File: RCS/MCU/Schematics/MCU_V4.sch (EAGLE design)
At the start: 28 parts, among them IC1 FT232RL, J1 MOTOR, J2 POWER, J3 SENSORS, Q2 8 MHz, U1 ATMEGA328P_TQFP

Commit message: Updated INTEV Schematic
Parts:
- added J5: USB-MICROB, SparkFun-Connectors:USB-MICROB
- added SW1: (no value), adafruit:SWITCH_PUSHBUTTONSOFTTOUCHSMD_SJ
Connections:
- net DM: now also J5.D-
- net DP: now also J5.D+
- net GND: now also J5.GND, SW1.P$2
- net RESET: now also SW1.P$1
- net USBVDD: now also J5.VBUS
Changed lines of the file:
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@@
 <part name="J3" library="SparkFun-Connectors" deviceset="M03" device="LOCK" value="SENSORS"/>
 <part name="J4" library="SparkFun-Connectors" deviceset="M06" device="LOCK"/>
+<part name="SW1" library="adafruit" deviceset="SWITCH_PUSHBUTTON" device="SOFTTOUCHSMD_SJ"/>
+<part name="GND13" library="supply1" deviceset="GND" device=""/>
+<part name="J5" library="SparkFun-Connectors" deviceset="USB" device="-MICROB"/>
+<part name="GND14" library="supply1" deviceset="GND" device=""/>
 </parts>
 <sheets>
@@
 <instance part="J3" gate="J$1" x="-12.7" y="78.74"/>
 <instance part="J4" gate="G$1" x="-40.64" y="86.36"/>
+<instance part="SW1" gate="G$1" x="43.18" y="88.9"/>
+<instance part="GND13" gate="1" x="91.44" y="81.28"/>
+<instance part="J5" gate="G$1" x="-45.72" y="45.72" rot="R180"/>
+<instance part="GND14" gate="1" x="-30.48" y="40.64"/>
 </instances>
 <busses>
@@
 <label x="-33.02" y="81.28" size="1.27" layer="95" xref="yes"/>
 </segment>
+<segment>
+<pinref part="GND13" gate="1" pin="GND"/>
+<wire x1="48.26" y1="88.9" x2="91.44" y2="88.9" width="0.1524" layer="91"/>
+<wire x1="91.44" y1="88.9" x2="91.44" y2="83.82" width="0.1524" layer="91"/>
+<pinref part="SW1" gate="G$1" pin="P$2"/>
+</segment>
+<segment>
+<pinref part="J5" gate="G$1" pin="GND"/>
+<wire x1="-43.18" y1="45.72" x2="-30.48" y2="45.72" width="0.1524" layer="91"/>
+<wire x1="-30.48" y1="45.72" x2="-30.48" y2="43.18" width="0.1524" layer="91"/>
+<pinref part="GND14" gate="1" pin="GND"/>
+</segment>
 </net>
 <net name="VDD" class="0">
@@
 <label x="111.76" y="7.62" size="1.27" layer="95" rot="R180" xref="yes"/>
 </segment>
+<segment>
+<pinref part="J5" gate="G$1" pin="D-"/>
+<wire x1="-43.18" y1="40.64" x2="-40.64" y2="40.64" width="0.1524" layer="91"/>
+<label x="-40.64" y="40.64" size="1.27" layer="95" xref="yes"/>
+</segment>
 </net>
 <net name="DP" class="0">
@@
 <wire x1="114.3" y1="10.16" x2="111.76" y2="10.16" width="0.1524" layer="91"/>
 <label x="111.76" y="10.16" size="1.27" layer="95" rot="R180" xref="yes"/>
+</segment>
+<segment>
+<pinref part="J5" gate="G$1" pin="D+"/>
+<wire x1="-43.18" y1="38.1" x2="-40.64" y2="38.1" width="0.1524" layer="91"/>
+<label x="-40.64" y="38.1" size="1.27" layer="95" xref="yes"/>
 </segment>
 </net>
@@
 <label x="-2.54" y="76.2" size="1.27" layer="95" xref="yes"/>
 <pinref part="J3" gate="J$1" pin="1"/>
-</segment>
-</net>
-<net name="N$5" class="0">
-<segment>
-<pinref part="FLIGHT-STATE-TABLE" gate="G$1" pin="A2"/>
-<wire x1="147.32" y1="104.14" x2="139.7" y2="104.14" width="0.1524" layer="91"/>
-<wire x1="147.32" y1="104.14" x2="147.32" y2="111.76" width="0.1524" layer="91"/>
-<pinref part="FLIGHT-STATE-TABLE" gate="G$1" pin="WP"/>
-<wire x1="139.7" y1="93.98" x2="152.4" y2="93.98" width="0.1524" layer="91"/>
-<wire x1="152.4" y1="93.98" x2="152.4" y2="111.76" width="0.1524" layer="91"/>
-<wire x1="152.4" y1="111.76" x2="147.32" y2="111.76" width="0.1524" layer="91"/>
-<pinref part="R1" gate="G$1" pin="2"/>
-<wire x1="147.32" y1="111.76" x2="116.84" y2="111.76" width="0.1524" layer="91"/>
-<wire x1="20.32" y1="86.36" x2="20.32" y2="88.9" width="0.1524" layer="91"/>
-<wire x1="20.32" y1="88.9" x2="20.32" y2="91.44" width="0.1524" layer="91"/>
-<wire x1="20.32" y1="88.9" x2="101.6" y2="88.9" width="0.1524" layer="91"/>
-<wire x1="101.6" y1="88.9" x2="101.6" y2="104.14" width="0.1524" layer="91"/>
-<junction x="20.32" y="88.9"/>
-<pinref part="FLIGHT-STATE-TABLE" gate="G$1" pin="VCC"/>
-<wire x1="101.6" y1="104.14" x2="116.84" y2="104.14" width="0.1524" layer="91"/>
-<pinref part="FLIGHT-DATA-STORAGE" gate="G$1" pin="VCC"/>
-<wire x1="116.84" y1="104.14" x2="119.38" y2="104.14" width="0.1524" layer="91"/>
-<wire x1="119.38" y1="76.2" x2="101.6" y2="76.2" width="0.1524" layer="91"/>
-<wire x1="101.6" y1="76.2" x2="101.6" y2="88.9" width="0.1524" layer="91"/>
-<junction x="101.6" y="88.9"/>
-<wire x1="116.84" y1="111.76" x2="116.84" y2="104.14" width="0.1524" layer="91"/>
-<junction x="116.84" y="104.14"/>
-<junction x="147.32" y="111.76"/>
-<pinref part="R4" gate="G$1" pin="2"/>
-<wire x1="10.16" y1="93.98" x2="15.24" y2="93.98" width="0.1524" layer="91"/>
-<wire x1="15.24" y1="93.98" x2="15.24" y2="88.9" width="0.1524" layer="91"/>
-<wire x1="15.24" y1="88.9" x2="20.32" y2="88.9" width="0.1524" layer="91"/>
-<wire x1="15.24" y1="88.9" x2="15.24" y2="68.58" width="0.1524" layer="91"/>
-<junction x="15.24" y="88.9"/>
-<pinref part="U1" gate="U$1" pin="VCC@6"/>
-<pinref part="U1" gate="U$1" pin="VCC@4"/>
-<pinref part="U1" gate="U$1" pin="AVCC"/>
-<wire x1="35.56" y1="68.58" x2="33.02" y2="68.58" width="0.1524" layer="91"/>
-<wire x1="33.02" y1="68.58" x2="33.02" y2="66.04" width="0.1524" layer="91"/>
-<wire x1="33.02" y1="66.04" x2="35.56" y2="66.04" width="0.1524" layer="91"/>
-<junction x="33.02" y="66.04"/>
-<wire x1="33.02" y1="66.04" x2="33.02" y2="63.5" width="0.1524" layer="91"/>
-<wire x1="33.02" y1="63.5" x2="35.56" y2="63.5" width="0.1524" layer="91"/>
-<wire x1="15.24" y1="68.58" x2="33.02" y2="68.58" width="0.1524" layer="91"/>
-<junction x="33.02" y="68.58"/>
-<pinref part="F1" gate="1" pin="1"/>
 </segment>
 </net>
@@
 <label x="106.68" y="43.18" size="1.27" layer="95" rot="R180" xref="yes"/>
 </segment>
+<segment>
+<pinref part="J5" gate="G$1" pin="VBUS"/>
+<wire x1="-43.18" y1="43.18" x2="-40.64" y2="43.18" width="0.1524" layer="91"/>
+<label x="-40.64" y="43.18" size="1.27" layer="95" xref="yes"/>
+</segment>
 </net>
 <net name="N$9" class="0">
@@
 <wire x1="33.02" y1="81.28" x2="50.8" y2="81.28" width="0.1524" layer="91"/>
 <junction x="33.02" y="73.66"/>
+<wire x1="33.02" y1="81.28" x2="33.02" y2="88.9" width="0.1524" layer="91"/>
+<junction x="33.02" y="81.28"/>
+<pinref part="SW1" gate="G$1" pin="P$1"/>
+<wire x1="33.02" y1="88.9" x2="38.1" y2="88.9" width="0.1524" layer="91"/>
 </segment>
 </net>
@@
 </segment>
 </net>
+<net name="N$1" class="0">
+<segment>
+<pinref part="U1" gate="U$1" pin="VCC@6"/>
+<wire x1="33.02" y1="63.5" x2="35.56" y2="63.5" width="0.1524" layer="91"/>
+<pinref part="U1" gate="U$1" pin="VCC@4"/>
+<wire x1="33.02" y1="66.04" x2="35.56" y2="66.04" width="0.1524" layer="91"/>
+<junction x="33.02" y="66.04"/>
+<wire x1="33.02" y1="66.04" x2="33.02" y2="63.5" width="0.1524" layer="91"/>
+<pinref part="U1" gate="U$1" pin="AVCC"/>
+<wire x1="35.56" y1="68.58" x2="33.02" y2="68.58" width="0.1524" layer="91"/>
+<wire x1="33.02" y1="68.58" x2="33.02" y2="66.04" width="0.1524" layer="91"/>
+<junction x="33.02" y="68.58"/>
+<pinref part="F1" gate="1" pin="1"/>
+<pinref part="R1" gate="G$1" pin="2"/>
+<wire x1="20.32" y1="86.36" x2="20.32" y2="88.9" width="0.1524" layer="91"/>
+<wire x1="20.32" y1="88.9" x2="20.32" y2="91.44" width="0.1524" layer="91"/>
+<junction x="20.32" y="88.9"/>
+<pinref part="R4" gate="G$1" pin="2"/>
+<wire x1="10.16" y1="93.98" x2="15.24" y2="93.98" width="0.1524" layer="91"/>
+<wire x1="15.24" y1="93.98" x2="15.24" y2="88.9" width="0.1524" layer="91"/>
+<wire x1="15.24" y1="88.9" x2="20.32" y2="88.9" width="0.1524" layer="91"/>
+<junction x="15.24" y="88.9"/>
+<wire x1="15.24" y1="88.9" x2="15.24" y2="68.58" width="0.1524" layer="91"/>
+<wire x1="15.24" y1="68.58" x2="33.02" y2="68.58" width="0.1524" layer="91"/>
+<wire x1="20.32" y1="88.9" x2="27.94" y2="88.9" width="0.1524" layer="91"/>
+<wire x1="27.94" y1="88.9" x2="27.94" y2="99.06" width="0.1524" layer="91"/>
+<pinref part="FLIGHT-STATE-TABLE" gate="G$1" pin="A2"/>
+<wire x1="147.32" y1="104.14" x2="139.7" y2="104.14" width="0.1524" layer="91"/>
+<wire x1="147.32" y1="104.14" x2="147.32" y2="111.76" width="0.1524" layer="91"/>
+<pinref part="FLIGHT-STATE-TABLE" gate="G$1" pin="WP"/>
+<wire x1="139.7" y1="93.98" x2="152.4" y2="93.98" width="0.1524" layer="91"/>
+<wire x1="152.4" y1="93.98" x2="152.4" y2="111.76" width="0.1524" layer="91"/>
+<wire x1="152.4" y1="111.76" x2="147.32" y2="111.76" width="0.1524" layer="91"/>
+<wire x1="147.32" y1="111.76" x2="116.84" y2="111.76" width="0.1524" layer="91"/>
+<wire x1="101.6" y1="76.2" x2="101.6" y2="99.06" width="0.1524" layer="91"/>
+<pinref part="FLIGHT-STATE-TABLE" gate="G$1" pin="VCC"/>
+<wire x1="101.6" y1="99.06" x2="101.6" y2="104.14" width="0.1524" layer="91"/>
+<wire x1="101.6" y1="104.14" x2="116.84" y2="104.14" width="0.1524" layer="91"/>
+<pinref part="FLIGHT-DATA-STORAGE" gate="G$1" pin="VCC"/>
+<wire x1="116.84" y1="104.14" x2="119.38" y2="104.14" width="0.1524" layer="91"/>
+<wire x1="119.38" y1="76.2" x2="101.6" y2="76.2" width="0.1524" layer="91"/>
+<wire x1="116.84" y1="111.76" x2="116.84" y2="104.14" width="0.1524" layer="91"/>
+<junction x="116.84" y="104.14"/>
+<junction x="147.32" y="111.76"/>
+<wire x1="27.94" y1="99.06" x2="101.6" y2="99.06" width="0.1524" layer="91"/>
+<junction x="101.6" y="99.06"/>
+</segment>
+</net>

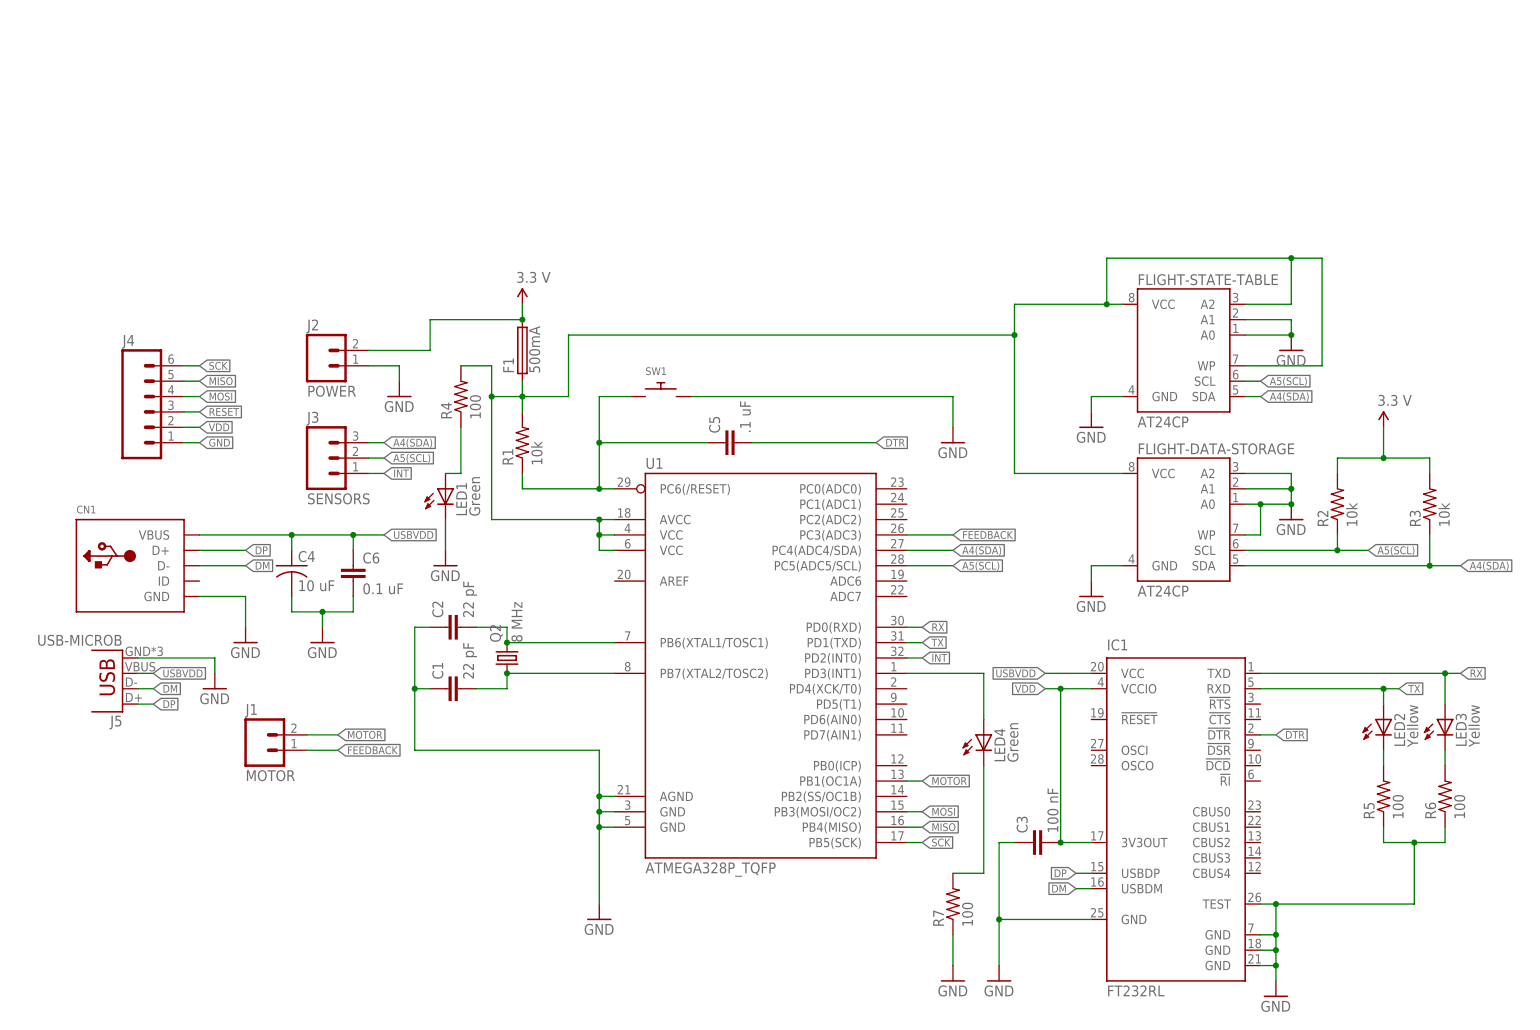
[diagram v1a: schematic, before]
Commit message: Updated MCU
Added adc, SPI connection, mini USB
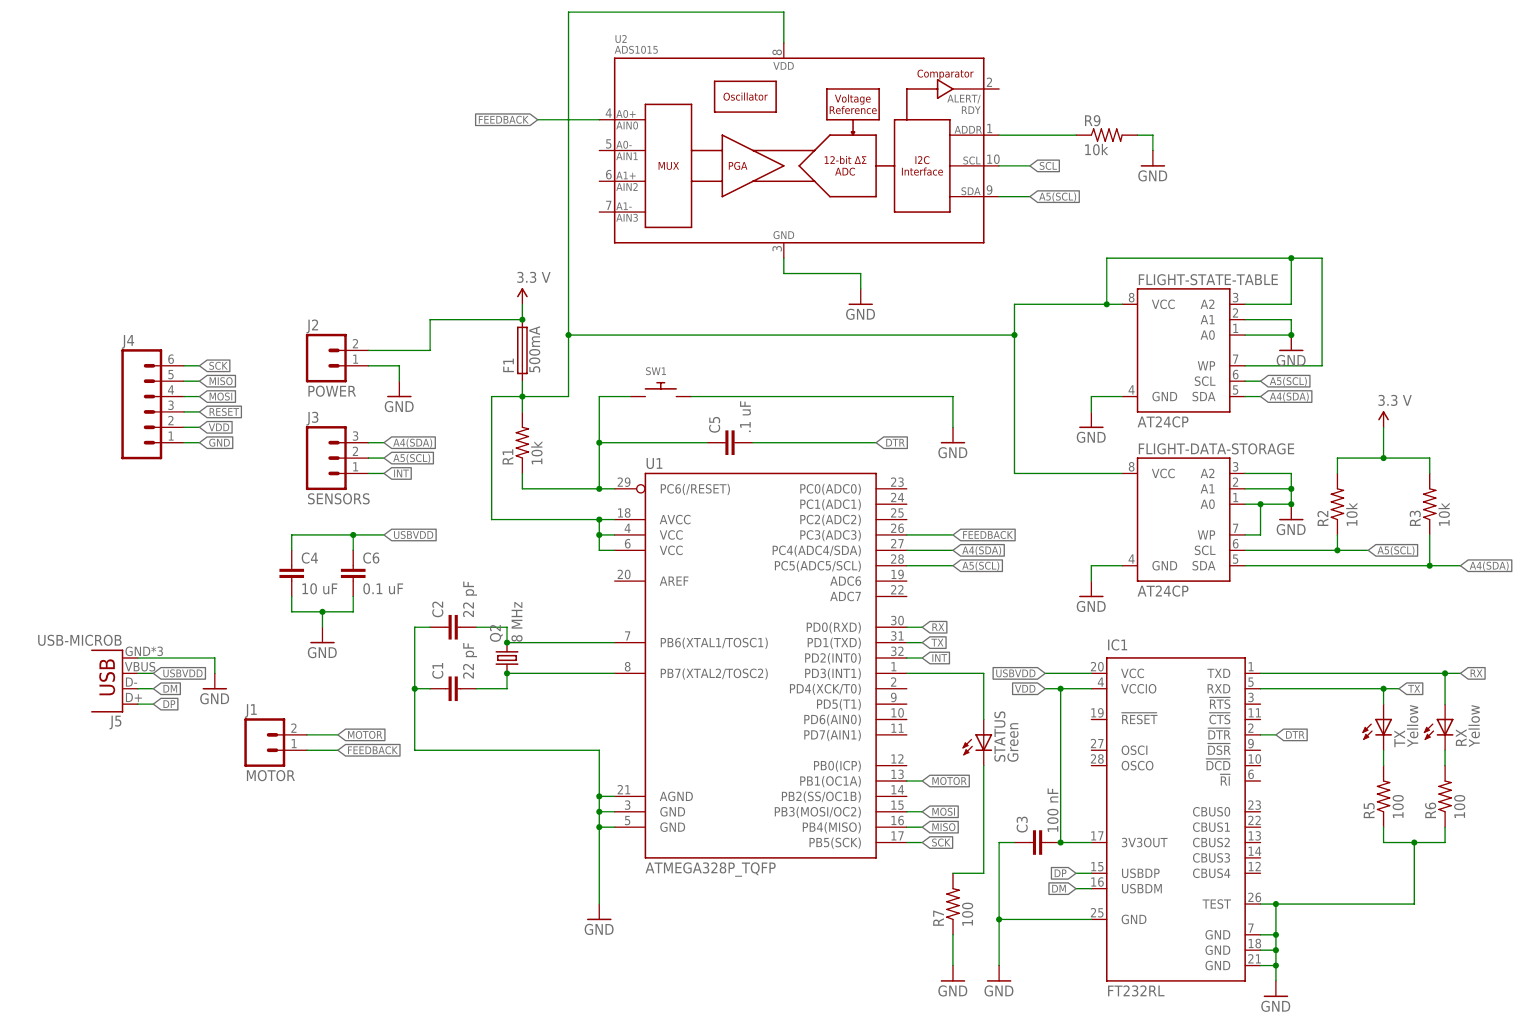
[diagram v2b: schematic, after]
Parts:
- removed CN1: (no value), adafruit:USBMOLEX
- removed LED1: Green, adafruit:LEDCHIPLED_1206
- removed R4: 100, adafruit:R-US_R1206
- added R9: 10k, adafruit:R-US_R1206
- added U2: ADS1015, SparkFun-AnalogIC:ADS1015
- C1, C2, C3, C5, C6: device capacitor-wima:C2,5-3 -> eagle-ltspice:CC1206
- C4: device adafruit:C-US025-024X044 -> eagle-ltspice:CC1206
- renumbered LED2 to TX, LED3 to RX, LED4 to STATUS
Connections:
- removed net N$6: LED1.A, R4.1
- new net SCL: U2.SCL
- net A4(SDA): now also R9.1, U2.ADDR
- net A5(SCL): now also U2.SDA
- net DM: no longer CN1.D-
- net DP: no longer CN1.D+
- net FEEDBACK: now also U2.AIN0
- net GND: now also R9.2, U2.VSS; no longer CN1.GND, LED1.C
- net N$1: now also U2.VDD; no longer R4.2
- net USBVDD: no longer CN1.VBUS
